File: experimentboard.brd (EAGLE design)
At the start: 109.2 x 100 mm, 173 parts, among them IC1 TL072P, IC2 LM317, IC3 LM337, IC4 TL072P, IC5 TL072P, IC6 TL072P, P1 PLR135/T9, P9 P9, U1 PCM1690, U2 DIR9001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

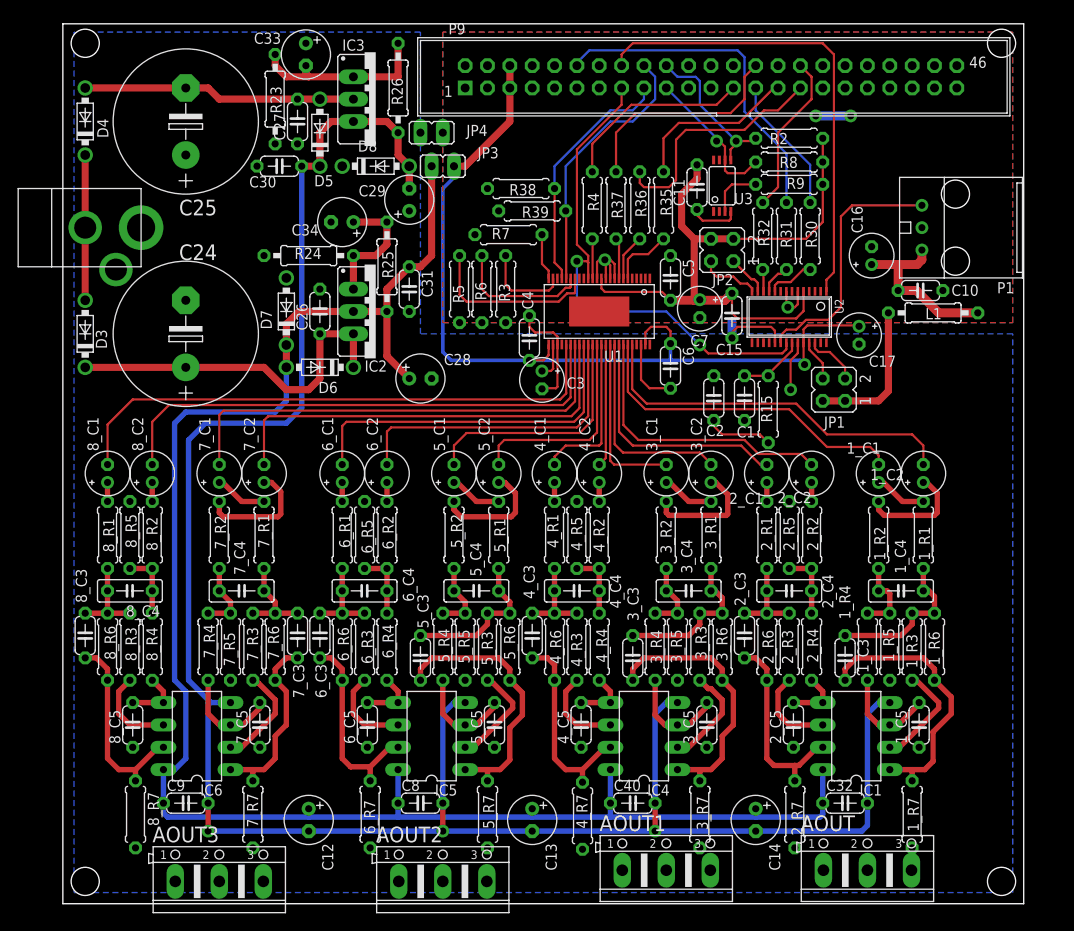
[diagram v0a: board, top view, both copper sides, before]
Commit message: Some moving around for DRC and one tiny airwire
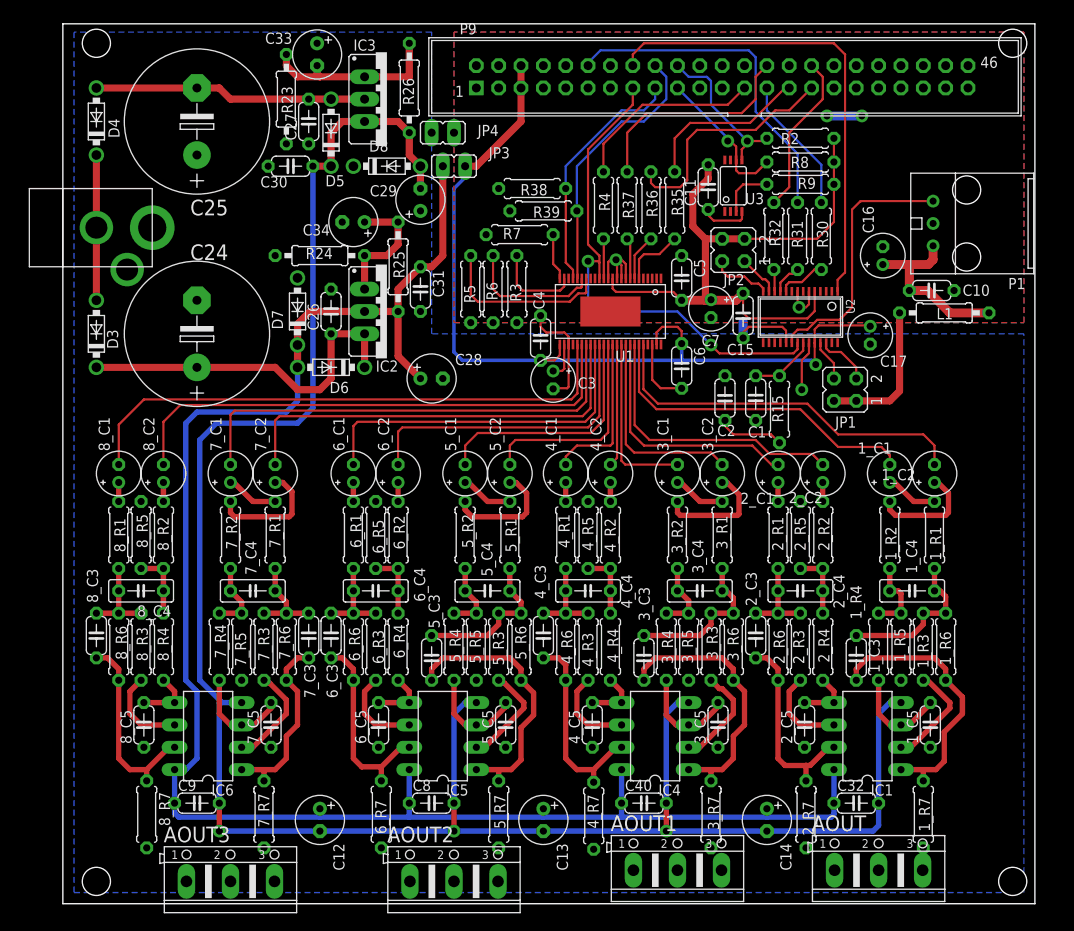
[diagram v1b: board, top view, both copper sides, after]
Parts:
- moved P1 1.36 mm to (110.3, 71.6)
- moved 1_C1 1.27 mm to (94.0, 48.9)
- moved 1_R2 1.27 mm to (94.0, 41.9)
- moved 1_R3 1.27 mm to (97.8, 29.2)
- moved 1_R7 1.27 mm to (97.8, 10.2)
- moved 3_C2 1.27 mm to (74.9, 48.9)
- moved 3_C3 1.27 mm to (66.0, 27.9)
- moved 3_R1 1.27 mm to (74.9, 41.9)
- moved 3_R5 1.27 mm to (71.1, 29.2)
- moved C10 1.27 mm to (98.7, 69.7)
- moved C14 1.27 mm to (80.0, 9.53)
- moved C40 1.27 mm to (66.0, 11.4)
- moved JP1 1.27 mm to (88.9, 58.4)
- moved 4_R7 1.27 mm to (60.3, 10.0)
- moved 5_R3 1.27 mm to (49.5, 29.2)
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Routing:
- net N$20: track 29.1 -> 29.7 mm
- net DGND: track 29.6 -> 30.2 mm
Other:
- board size 109.2 x 100 mm -> 110.5 x 100 mm

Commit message: Fixed DIR9001 VCC 3.3V misunderstanding
VCC is actually 3.3V, and AGND is only different from GND in where the
FILT ties. Almost have that complete. Need to tie the AGND to DGND
first, and not at a common point with the filter.
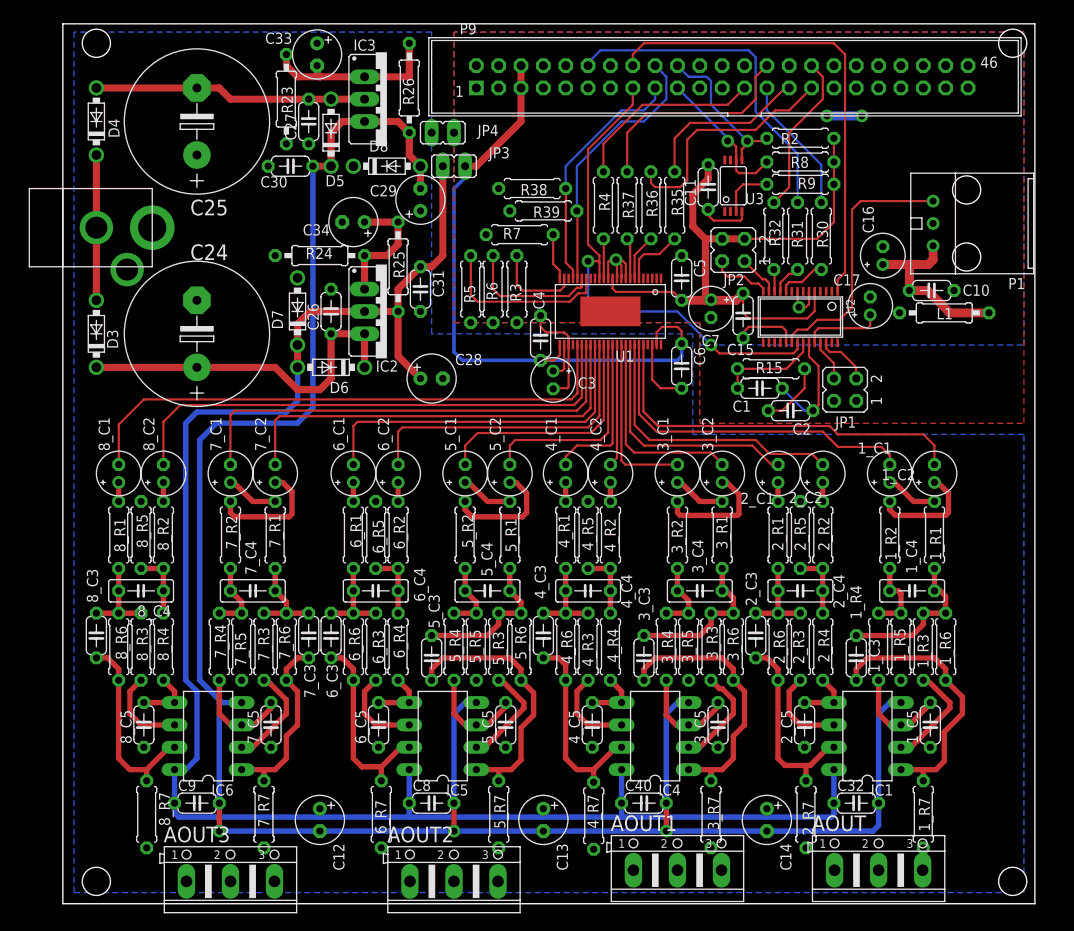
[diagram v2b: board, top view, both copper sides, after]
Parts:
- moved C2 7.60 mm to (82.7, 56.0), turned to 180 degrees
- moved R15 4.70 mm to (80.5, 60.8), turned to 0 degrees
- moved C17 3.33 mm to (91.8, 67.9), turned to 90 degrees
- moved C1 1.21 mm to (79.2, 58.6), turned to 180 degrees
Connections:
- net N$4 renamed FILT
- net AGND: no longer C1.1, C17.-, C2.1, U2.23
- net DGND: now also C1.1, C17.-, C2.1, U2.23
- net VCC: no longer C17.+, U2.24
- net VDD: now also C17.+, U2.24
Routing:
- net VCC: track 100.5 -> 74.1 mm, vias 1 -> 0
- net DGND: track 30.2 -> 41.3 mm
- net VDD: track 92.3 -> 84.5 mm
- net AGND: track 25.9 -> 20.2 mm, vias 1 -> 0
- net FILT: track 7.57 -> 11.5 mm
- net VOUT1+: track 37.9 -> 39.4 mm
- net VOUT1-: track 43.0 -> 44.5 mm

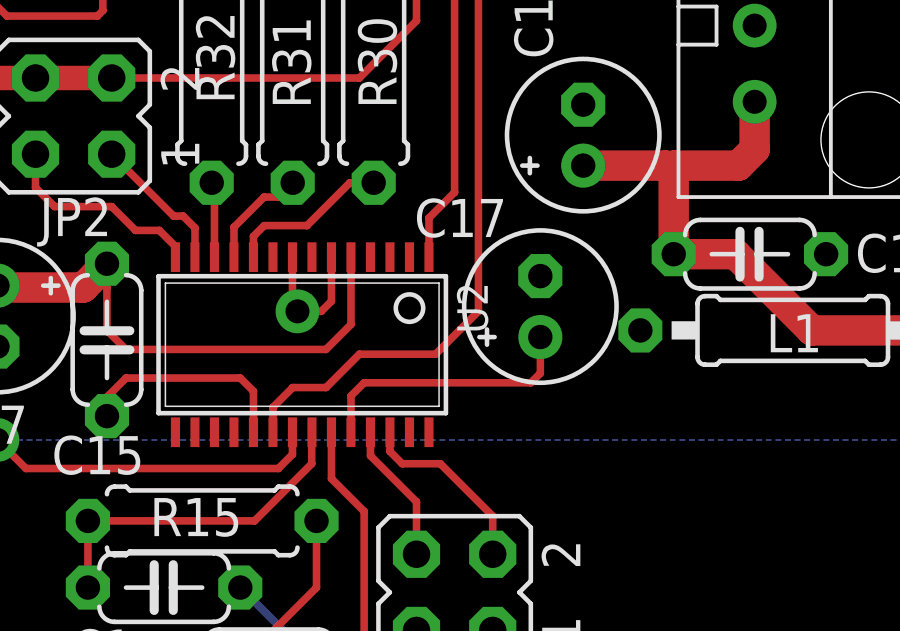
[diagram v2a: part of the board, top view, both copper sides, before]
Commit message: Gave FILT on DIR9001 a dedicated gnd
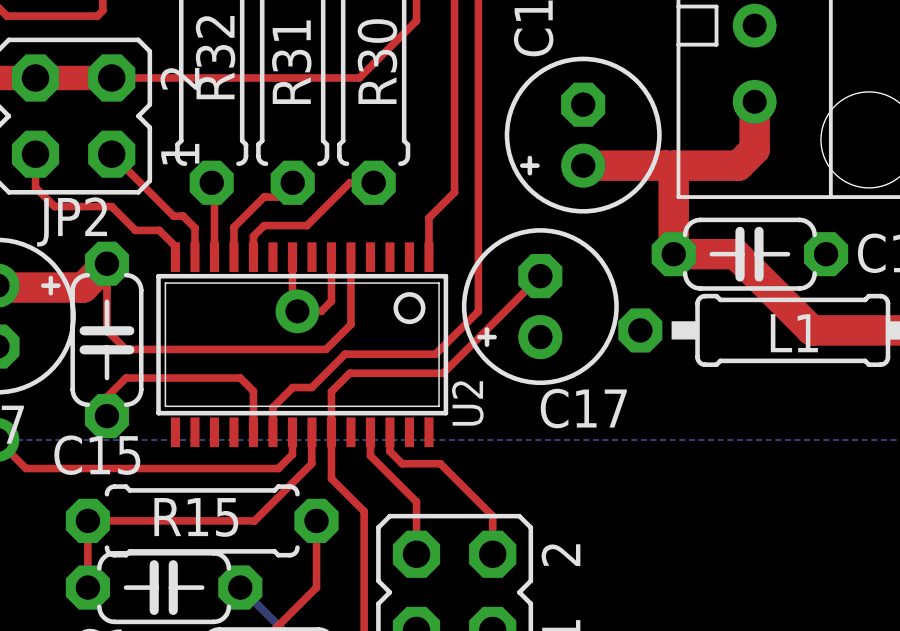
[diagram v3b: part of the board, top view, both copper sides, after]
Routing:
- net DGND: track 41.3 -> 51.2 mm
- net VDD: track 84.5 -> 75.5 mm
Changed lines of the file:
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@@
 <attribute name="VALUE" x="30.353" y="80.137" size="1.27" layer="27" ratio="10" rot="R180"/>
 </element>
-<element name="U2" library="0000halfgaar" package="TSSOP28" value="DIR9001" x="83.82" y="66.675" rot="R180"/>
+<element name="U2" library="0000halfgaar" package="TSSOP28" value="DIR9001" x="83.82" y="66.675" smashed="yes" rot="R180">
+<attribute name="NAME" x="88.83185" y="65.5828" size="1.016" layer="25" ratio="10" rot="R270"/>
+<attribute name="VALUE" x="77.6588" y="68.7578" size="1.016" layer="27" ratio="10" rot="R270"/>
+</element>
 <element name="C1" library="rcl" package="C050-024X044" value="4.7n" x="79.21625" y="58.57875" smashed="yes" rot="R180">
 <attribute name="NAME" x="78.20025" y="57.18175" size="1.27" layer="25" ratio="10" rot="R180"/>
@@
 <element name="C16" library="rcl" package="E2-5" value="10 µF" x="93.18625" y="73.66" rot="R90"/>
 <element name="C17" library="rcl" package="E2-5" value="10 µF" x="91.7575" y="67.945" smashed="yes" rot="R90">
-<attribute name="NAME" x="90.64625" y="71.53275" size="1.27" layer="25" ratio="10" rot="R180"/>
+<attribute name="NAME" x="94.77375" y="65.18275" size="1.27" layer="25" ratio="10" rot="R180"/>
 <attribute name="VALUE" x="93.9165" y="70.485" size="1.27" layer="27" ratio="10" rot="R90"/>
 </element>
@@
 <contactref element="U2" pad="24"/>
 <contactref element="C17" pad="+"/>
-<wire x1="85.445" y1="63.7572" x2="85.445" y2="64.96625" width="0.254" layer="1"/>
-<wire x1="85.445" y1="64.96625" x2="85.88375" y2="65.405" width="0.254" layer="1"/>
-<wire x1="85.88375" y1="65.405" x2="91.44" y2="65.405" width="0.254" layer="1"/>
-<wire x1="91.44" y1="65.405" x2="91.7575" y2="65.7225" width="0.254" layer="1"/>
-<wire x1="91.7575" y1="65.7225" x2="91.7575" y2="66.929" width="0.254" layer="1"/>
 </signal>
 <signal name="DGND">
@@
 <wire x1="85.88375" y1="61.11875" x2="85.88375" y2="56.67375" width="0.254" layer="1"/>
 <wire x1="85.88375" y1="56.67375" x2="85.24875" y2="56.03875" width="0.254" layer="1"/>
-<wire x1="82.195" y1="63.7572" x2="84.795" y2="63.7572" width="0" layer="19" extent="1-1"/>
+<wire x1="84.795" y1="63.7572" x2="84.795" y2="65.11" width="0.254" layer="1"/>
+<wire x1="85.4075" y1="65.7225" x2="88.519" y2="65.7225" width="0.254" layer="1"/>
+<wire x1="88.519" y1="65.7225" x2="91.7575" y2="68.961" width="0.254" layer="1"/>
+<wire x1="84.795" y1="65.11" x2="85.4075" y2="65.7225" width="0.254" layer="1"/>
 </signal>
 <signal name="AGND">
@@
 <wire x1="89.69375" y1="78.89875" x2="89.69375" y2="67.78625" width="0.254" layer="1"/>
 <wire x1="82.845" y1="63.7572" x2="82.845" y2="64.58875" width="0.254" layer="1"/>
-<wire x1="82.845" y1="64.58875" x2="83.5025" y2="65.24625" width="0.254" layer="1"/>
-<wire x1="83.5025" y1="65.24625" x2="84.61375" y2="65.24625" width="0.254" layer="1"/>
-<wire x1="84.61375" y1="65.24625" x2="85.725" y2="66.3575" width="0.254" layer="1"/>
-<wire x1="85.725" y1="66.3575" x2="88.265" y2="66.3575" width="0.254" layer="1"/>
+<wire x1="85.24875" y1="66.3575" x2="88.265" y2="66.3575" width="0.254" layer="1"/>
 <wire x1="90.64625" y1="79.85125" x2="89.69375" y2="78.89875" width="0.254" layer="1"/>
+<wire x1="85.24875" y1="66.3575" x2="84.1375" y2="65.24625" width="0.254" layer="1"/>
+<wire x1="84.1375" y1="65.24625" x2="83.5025" y2="65.24625" width="0.254" layer="1"/>
+<wire x1="83.5025" y1="65.24625" x2="82.845" y2="64.58875" width="0.254" layer="1"/>
 </signal>
 <signal name="MCLK">

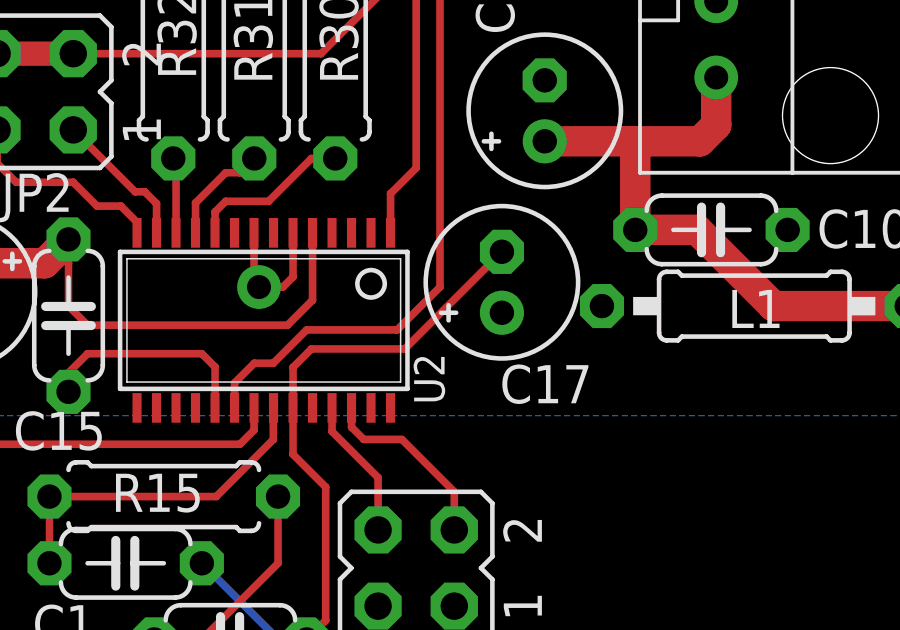
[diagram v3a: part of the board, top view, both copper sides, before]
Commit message: Removed unnecessary decoupling cap
I had added it to decouple VCC to DIR9001, but it didn't even need VCC,
that was a bug.
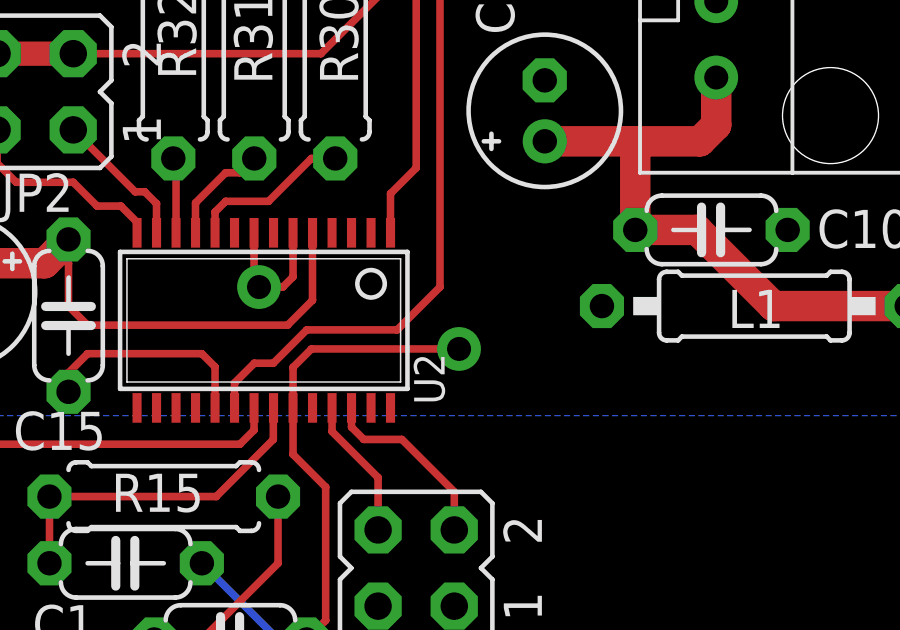
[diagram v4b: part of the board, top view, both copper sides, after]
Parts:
- removed C17: 10 µF, rcl:E2-5
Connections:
- net DGND: no longer C17.-
- net VDD: no longer C17.+
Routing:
- net DGND: track 51.2 -> 48.4 mm, vias 2 -> 3
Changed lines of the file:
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@@
 </element>
 <element name="C16" library="rcl" package="E2-5" value="10 µF" x="93.18625" y="73.66" rot="R90"/>
-<element name="C17" library="rcl" package="E2-5" value="10 µF" x="91.7575" y="67.945" smashed="yes" rot="R90">
-<attribute name="NAME" x="94.77375" y="65.18275" size="1.27" layer="25" ratio="10" rot="R180"/>
-<attribute name="VALUE" x="93.9165" y="70.485" size="1.27" layer="27" ratio="10" rot="R90"/>
-</element>
 <element name="JP4" library="jumper" package="JP1" value="" x="43.18" y="87.63" smashed="yes" rot="R90">
 <attribute name="NAME" x="49.53" y="88.519" size="1.27" layer="25" ratio="10" rot="R180"/>
@@
 <wire x1="86.83625" y1="89.535" x2="90.805" y2="89.535" width="1.016" layer="16"/>
 <contactref element="U2" pad="24"/>
-<contactref element="C17" pad="+"/>
 </signal>
 <signal name="DGND">
@@
 <wire x1="77.94625" y1="65.56375" x2="77.31125" y2="64.92875" width="0.254" layer="1"/>
 <wire x1="77.31125" y1="64.92875" x2="77.31125" y2="64.29375" width="0.254" layer="1"/>
-<contactref element="C17" pad="-"/>
 <contactref element="U2" pad="23"/>
 <contactref element="C1" pad="1"/>
@@
 <wire x1="85.88375" y1="56.67375" x2="85.24875" y2="56.03875" width="0.254" layer="1"/>
 <wire x1="84.795" y1="63.7572" x2="84.795" y2="65.11" width="0.254" layer="1"/>
-<wire x1="85.4075" y1="65.7225" x2="88.519" y2="65.7225" width="0.254" layer="1"/>
-<wire x1="88.519" y1="65.7225" x2="91.7575" y2="68.961" width="0.254" layer="1"/>
+<wire x1="85.4075" y1="65.7225" x2="90.32875" y2="65.7225" width="0.254" layer="1"/>
 <wire x1="84.795" y1="65.11" x2="85.4075" y2="65.7225" width="0.254" layer="1"/>
+<via x="90.32875" y="65.7225" extent="1-16" drill="0.8" shape="octagon"/>
 </signal>
 <signal name="AGND">
